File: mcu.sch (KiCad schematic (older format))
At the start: 29 parts, among them IC2 LPC55S16JBD64E, Y1 16 MHz, Y2 32.768 kHz

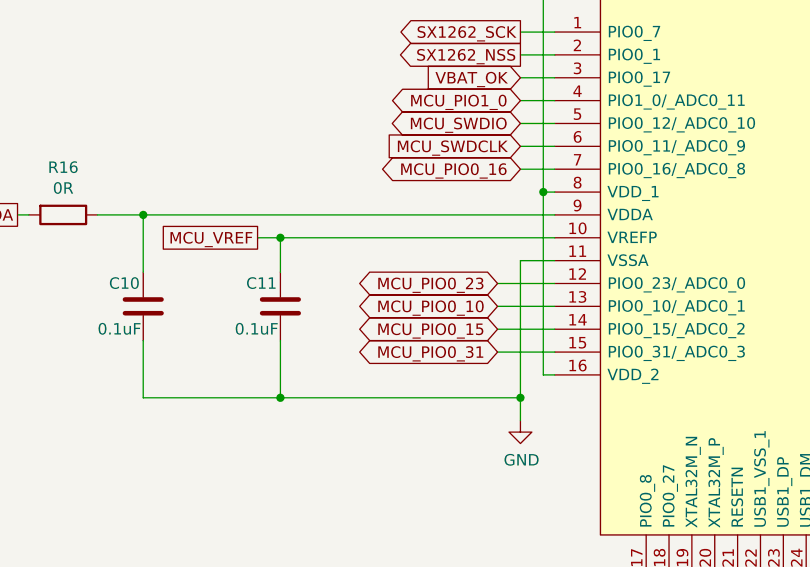
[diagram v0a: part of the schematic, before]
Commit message: Fixed issue #2, #3, #4 and #5
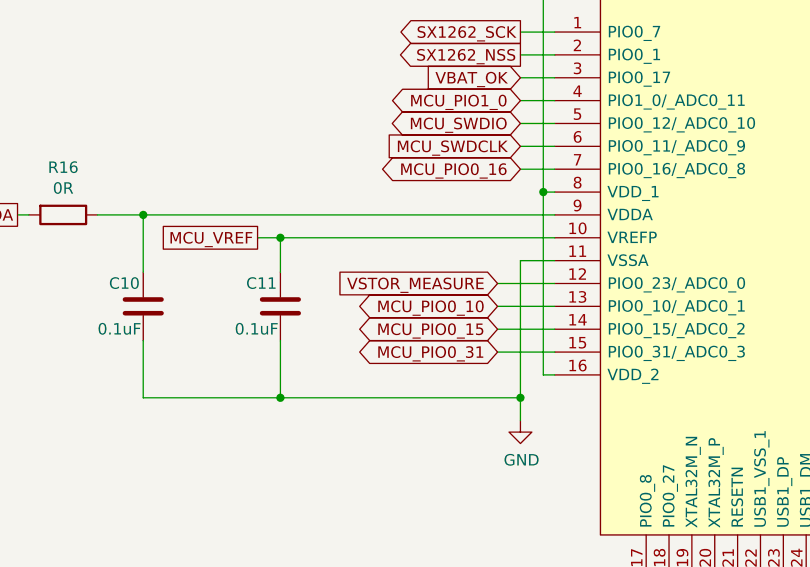
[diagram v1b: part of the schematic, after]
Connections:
- net MCU_PIO0_23 renamed VSTOR_MEASURE
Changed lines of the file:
@@
 Sheet 3 6
 Title "Tardigrade"
-Date "2020-09-24"
+Date "2020-11-05"
 Rev "1.0"
 Comp "Lucerne University of Applied Sciences and Arts"
@@
 Wire Wire Line
 	1150 1000 1150 1100
-Text GLabel 3350 4000 0    50   BiDi ~ 0
-MCU_PIO0_23
+Text GLabel 3350 4000 0    50   Input ~ 0
+VSTOR_MEASURE
 Wire Wire Line
 	6000 4300 7050 4300

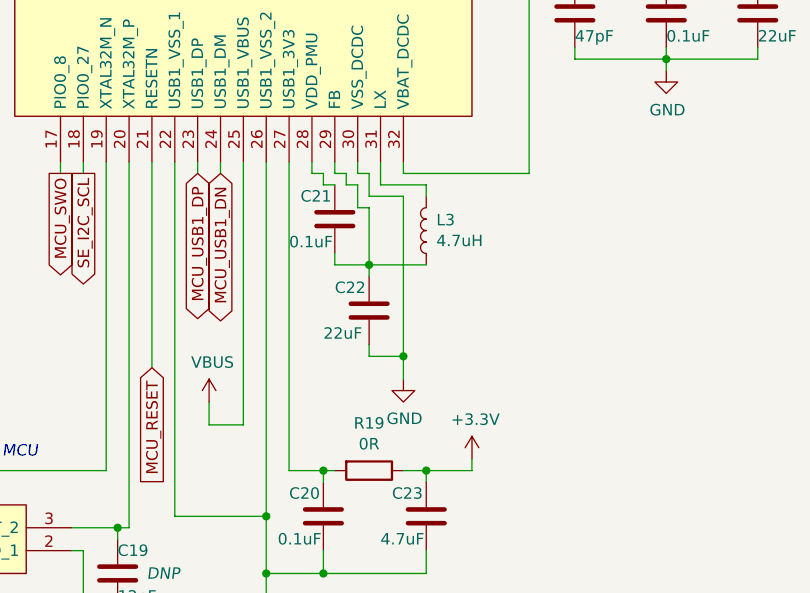
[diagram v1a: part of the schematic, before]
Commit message: Issue #6 - Fixed wrong placement of C21
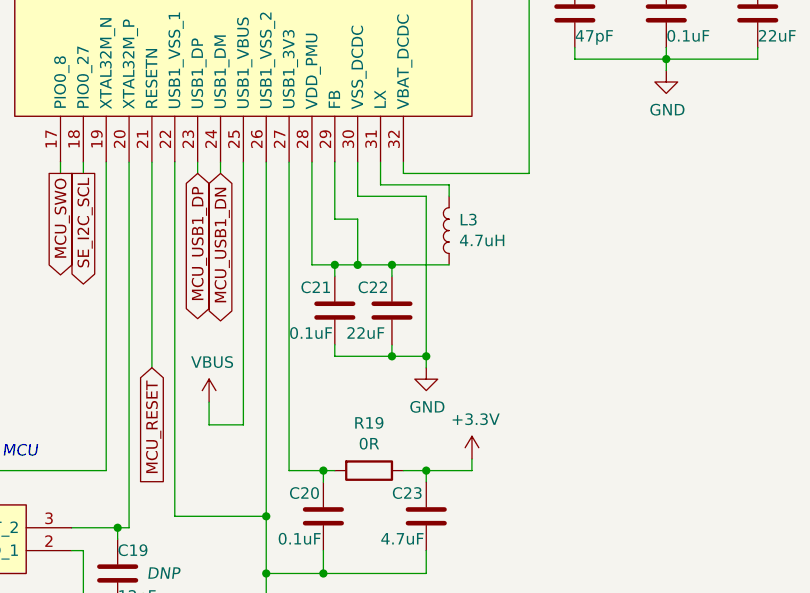
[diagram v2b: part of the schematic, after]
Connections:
- net GND: now also C21.2
- net at C21.1, IC2.28 (VDD_PMU): now also C22.1, IC2.29 (FB), L3.1
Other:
- moved on the sheet: C21, C22, L3
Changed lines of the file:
@@
-	1    0    0    -1
-$EndComp
-Connection ~ 5350 5750
-Wire Wire Line
-	5500 6150 5500 6250
-Wire Wire Line
-	5350 6150 5500 6150
-Wire Wire Line
-	5350 6100 5350 6150
-Wire Wire Line
-	5350 5750 5350 5800
-$Comp
-L Device:C C22
-U 1 1 5F6E64FA
-P 5350 5950
-F 0 "C22" H 5200 6050 50  0000 L CNN
-F 1 "22uF" H 5150 5850 50  0000 L CNN
-F 2 "Capacitor_SMD:C_0402_1005Metric" H 5388 5800 50  0001 C CNN
-F 3 "~" H 5350 5950 50  0001 C CNN
-	1    5350 5950
-	1    0    0    -1
-$EndComp
-$Comp
-L power:GND #PWR030
-U 1 1 5F6E76C2
-P 5500 6250
-F 0 "#PWR030" H 5500 6000 50  0001 C CNN
-F 1 "GND" H 5505 6077 50  0000 C CNN
-F 2 "" H 5500 6250 50  0001 C CNN
-F 3 "" H 5500 6250 50  0001 C CNN
-	1    5500 6250
 	1    0    0    -1
 $EndComp
 Wire Wire Line
 	5400 5300 5400 5400
-$Comp
-L Device:L L3
-U 1 1 5F6E59A5
-P 5600 5600
-F 0 "L3" H 5556 5554 50  0000 R CNN
-F 1 "4.7uH" H 5556 5645 50  0000 R CNN
-F 2 "Inductor_SMD:L_0402_1005Metric" H 5600 5600 50  0001 C CNN
-F 3 "~" H 5600 5600 50  0001 C CNN
-	1    5600 5600
-	-1   0    0    1
-$EndComp
-Wire Wire Line
-	5350 5750 5600 5750
-Wire Wire Line
-	5400 5400 5600 5400
-Wire Wire Line
-	5600 5400 5600 5450
-Wire Wire Line
-	5500 5450 5500 6150
-Connection ~ 5500 6150
-Wire Wire Line
-	5200 5300 5200 5350
-Wire Wire Line
-	5200 5350 5250 5350
-Wire Wire Line
-	5300 5300 5300 5350
-Wire Wire Line
-	5300 5350 5350 5350
-Wire Wire Line
-	5350 5350 5350 5450
-Wire Wire Line
-	5350 5450 5500 5450
-Wire Wire Line
-	5250 5350 5250 5400
-Wire Wire Line
-	5250 5400 5300 5400
-Wire Wire Line
-	5300 5400 5300 5500
-Wire Wire Line
-	5300 5500 5350 5500
-$Comp
-L Device:C C21
-U 1 1 5F6E300F
-P 5200 5550
-F 0 "C21" H 5050 5650 50  0000 L CNN
-F 1 "0.1uF" H 5000 5450 50  0000 L CNN
-F 2 "Capacitor_SMD:C_0402_1005Metric" H 5238 5400 50  0001 C CNN
-F 3 "~" H 5200 5550 50  0001 C CNN
-	1    5200 5550
-	1    0    0    -1
-$EndComp
-Wire Wire Line
-	5350 5500 5350 5750
-Wire Wire Line
-	5200 5700 5200 5750
-Wire Wire Line
-	5200 5750 5350 5750
-Wire Wire Line
-	5100 5300 5100 5350
-Wire Wire Line
-	5100 5350 5150 5350
-Wire Wire Line
-	5150 5350 5150 5400
-Wire Wire Line
-	5150 5400 5200 5400
 Wire Wire Line
 	4900 6850 4900 7100
@@
 Wire Wire Line
 	1150 1000 1150 1100
-Text GLabel 3350 4000 0    50   Input ~ 0
-VSTOR_MEASURE
 Wire Wire Line
 	6000 4300 7050 4300
@@
 Wire Wire Line
 	2100 1850 2050 1850
+$Comp
+L Device:C C21
+U 1 1 5F6E300F
+P 5200 5950
+F 0 "C21" H 5050 6050 50  0000 L CNN
+F 1 "0.1uF" H 5000 5850 50  0000 L CNN
+F 2 "Capacitor_SMD:C_0402_1005Metric" H 5238 5800 50  0001 C CNN
+F 3 "~" H 5200 5950 50  0001 C CNN
+	1    5200 5950
+	1    0    0    -1
+$EndComp
+$Comp
+L Device:C C22
+U 1 1 5F6E64FA
+P 5450 5950
+F 0 "C22" H 5300 6050 50  0000 L CNN
+F 1 "22uF" H 5250 5850 50  0000 L CNN
+F 2 "Capacitor_SMD:C_0402_1005Metric" H 5488 5800 50  0001 C CNN
+F 3 "~" H 5450 5950 50  0001 C CNN
+	1    5450 5950
+	1    0    0    -1
+$EndComp
+$Comp
+L power:GND #PWR030
+U 1 1 5F6E76C2
+P 5600 6200
+F 0 "#PWR030" H 5600 5950 50  0001 C CNN
+F 1 "GND" H 5605 6027 50  0000 C CNN
+F 2 "" H 5600 6200 50  0001 C CNN
+F 3 "" H 5600 6200 50  0001 C CNN
+	1    5600 6200
+	1    0    0    -1
+$EndComp
+$Comp
+L Device:L L3
+U 1 1 5F6E59A5
+P 5700 5600
+F 0 "L3" H 5656 5554 50  0000 R CNN
+F 1 "4.7uH" H 5656 5645 50  0000 R CNN
+F 2 "Inductor_SMD:L_0402_1005Metric" H 5700 5600 50  0001 C CNN
+F 3 "~" H 5700 5600 50  0001 C CNN
+	1    5700 5600
+	-1   0    0    1
+$EndComp
+Text GLabel 3350 4000 0    50   Input ~ 0
+VSTOR_MEASURE
+Wire Wire Line
+	5700 5400 5700 5450
+Wire Wire Line
+	5400 5400 5700 5400
+Wire Wire Line
+	5200 5750 5200 5800
+Wire Wire Line
+	5100 5300 5100 5750
+Wire Wire Line
+	5100 5750 5200 5750
+Connection ~ 5200 5750
+Wire Wire Line
+	5450 5800 5450 5750
+Connection ~ 5450 5750
+Wire Wire Line
+	5450 5750 5700 5750
+Wire Wire Line
+	5200 5750 5300 5750
+Wire Wire Line
+	5200 5300 5200 5550
+Wire Wire Line
+	5200 5550 5300 5550
+Wire Wire Line
+	5300 5550 5300 5750
+Connection ~ 5300 5750
+Wire Wire Line
+	5300 5750 5450 5750
+Wire Wire Line
+	5600 6200 5600 6150
+Wire Wire Line
+	5600 5450 5300 5450
+Wire Wire Line
+	5300 5450 5300 5300
+Wire Wire Line
+	5200 6100 5200 6150
+Wire Wire Line
+	5200 6150 5450 6150
+Connection ~ 5600 6150
+Wire Wire Line
+	5600 6150 5600 5450
+Wire Wire Line
+	5450 6100 5450 6150
+Connection ~ 5450 6150
+Wire Wire Line
+	5450 6150 5600 6150
 $EndSCHEMATC

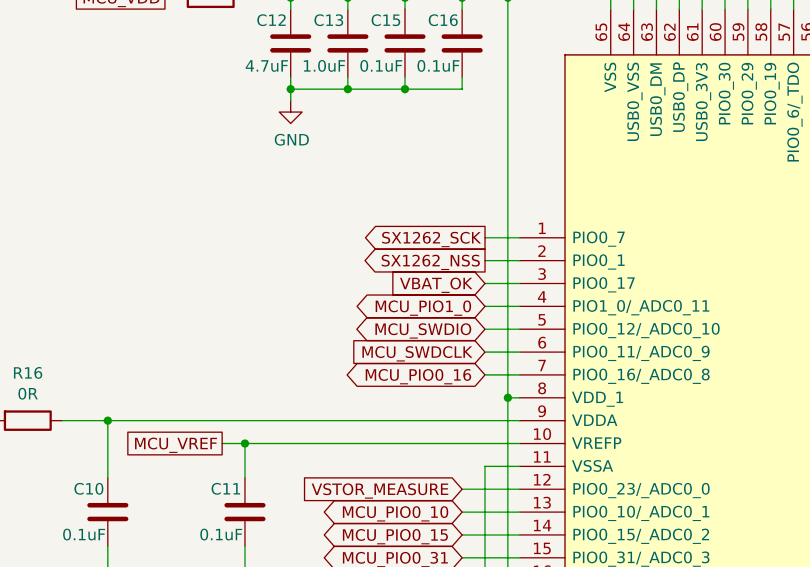
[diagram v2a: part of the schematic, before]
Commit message: Removed BAT_OK signal from MCU
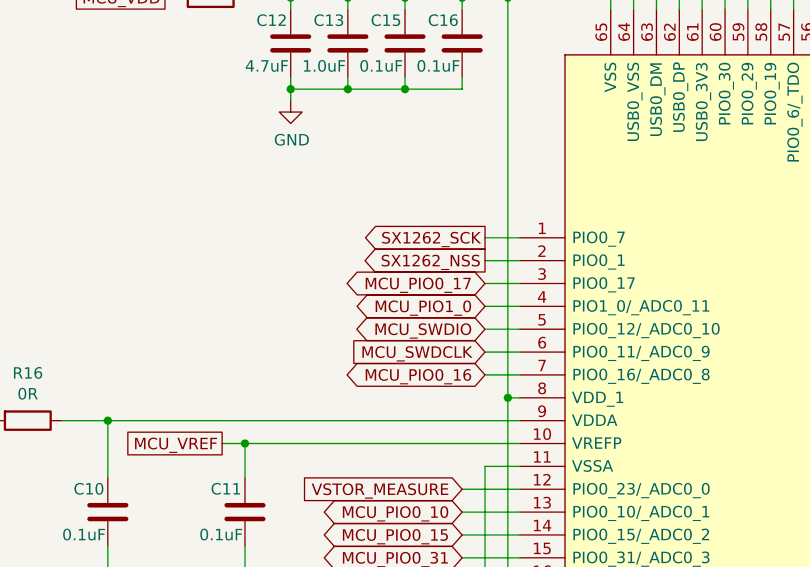
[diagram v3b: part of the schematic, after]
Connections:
- net VBAT_OK renamed MCU_PIO0_17
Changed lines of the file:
@@
 Text GLabel 6150 4100 2    50   Input ~ 0
 GNSS_PPS
-Text GLabel 3450 3100 0    50   Input ~ 0
-VBAT_OK
 Wire Wire Line
 	5000 1750 5000 1900
@@
 Wire Wire Line
 	5450 6150 5600 6150
+Text GLabel 3450 3100 0    50   BiDi ~ 0
+MCU_PIO0_17
 $EndSCHEMATC
